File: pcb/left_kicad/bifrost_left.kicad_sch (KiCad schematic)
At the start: 65 parts, among them J1 HRO_TYPE-C-31-M-12, J2 Conn_01x02, J3 Conn_01x06, Q1 AO3401A, Q2 2N7002, Q3 AO3401A, SW1 1.5U, SW10 SW_Push, SW11 SW_Push, SW12 1.25U, SW13 SW_Push, SW14 SW_Push, SW15 SW_Push, SW16 SW_Push, SW17 SW_Push, SW18 SW_Push, SW19 SW_Push, SW2 1.75U, SW20 SW_Push, SW21 SW_Push, SW3 SW_Push, SW4 1.25U, SW5 SW_Push, SW6 SW_Push, SW7 SW_Push, SW8 1.25U, SW9 SW_Push, T1 SW_Push_Shielded, U1 MDBT50Q-1MV2, U2 TP4057, U3 SRV05-4, X1 32.768kHz

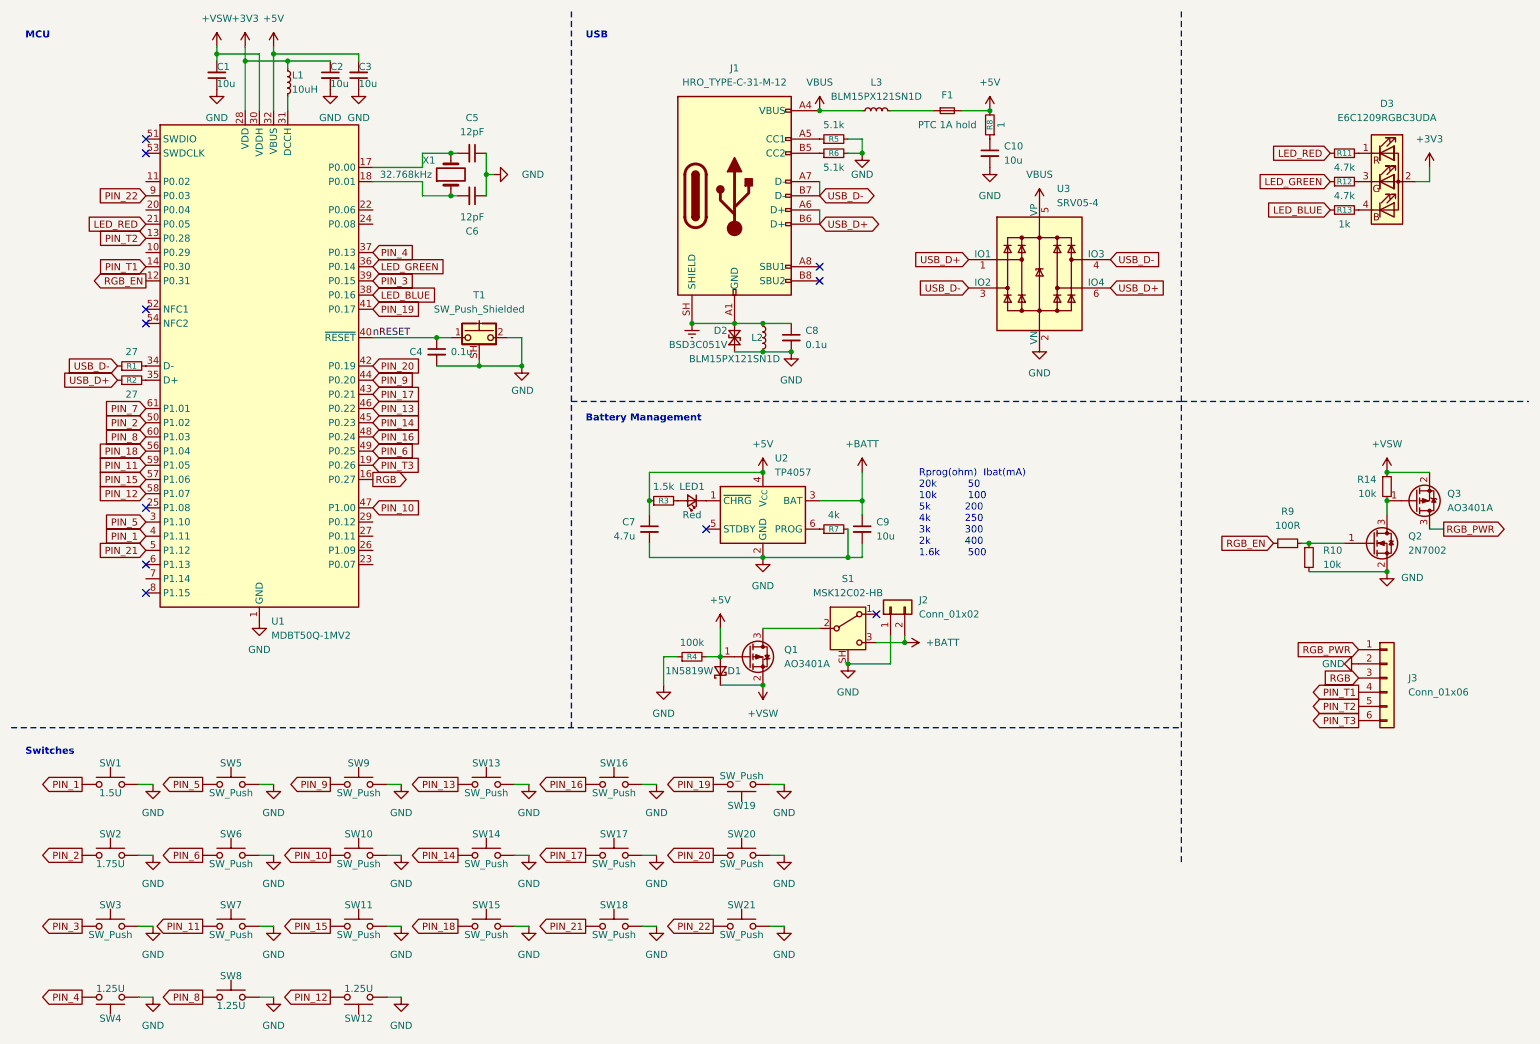
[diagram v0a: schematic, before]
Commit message: Update KiCad keyboard designs
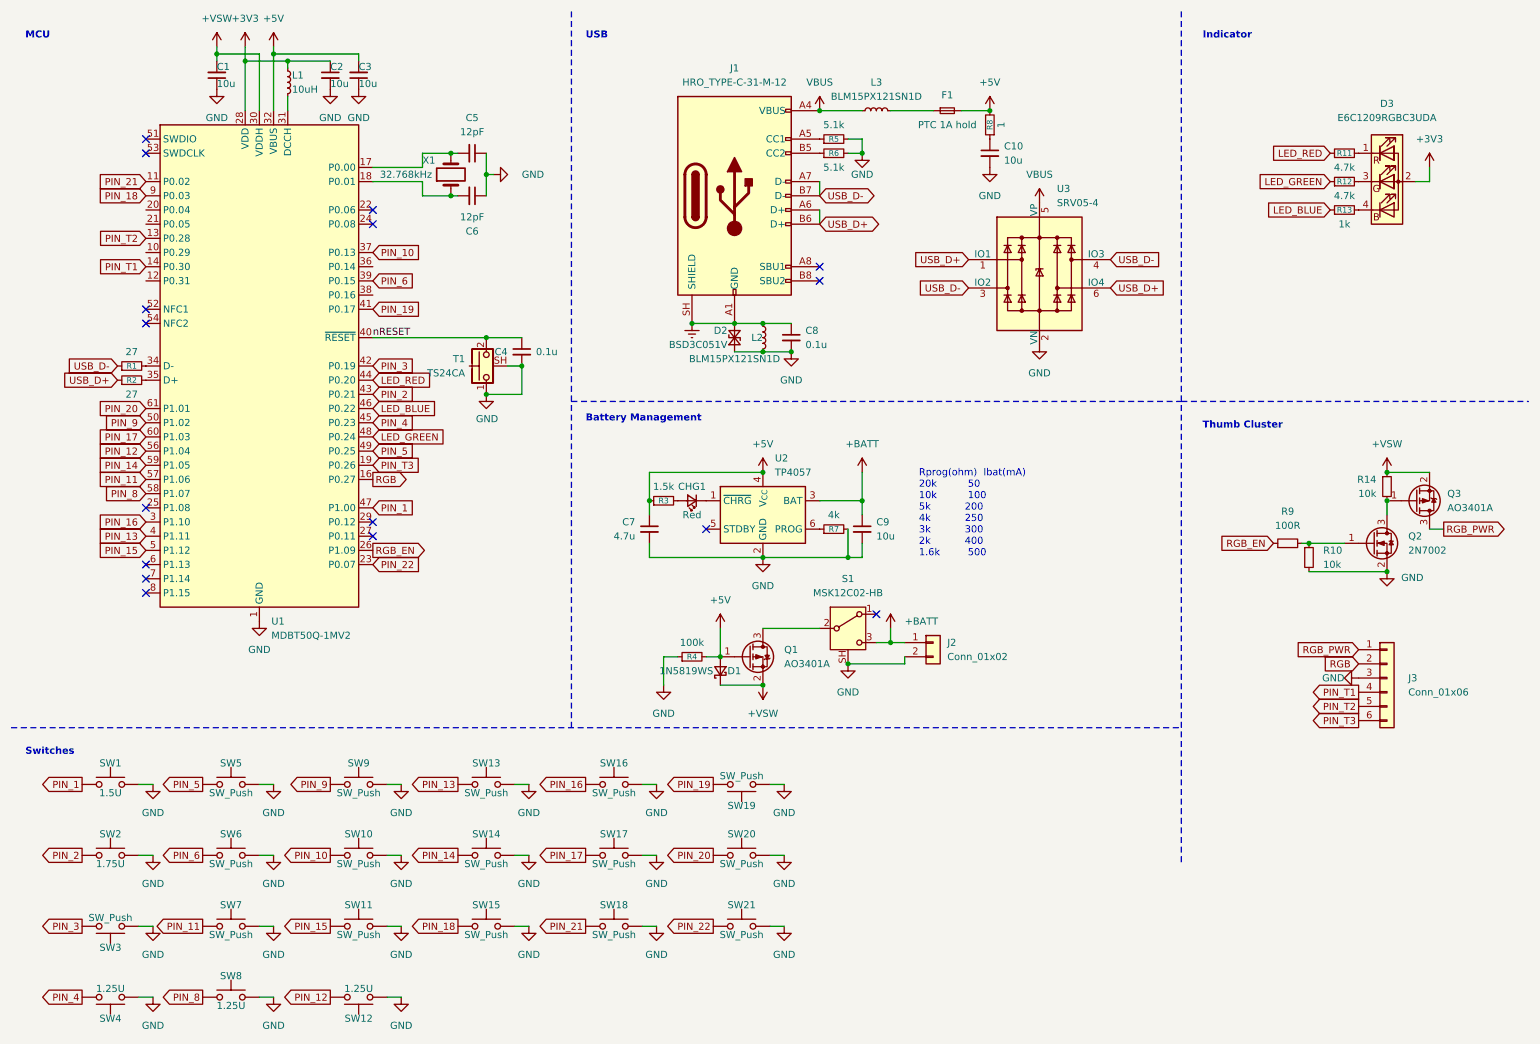
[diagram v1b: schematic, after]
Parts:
- D1: value 1N5819W -> 1N5819WS; footprint Diode_SMD:D_SOD-123 -> Diode_SMD:D_SOD-323
- J2: footprint Connector_Molex:Molex_PicoBlade_53398-0271_1x02-1MP_P1.25mm_Vertical -> Connector_PinHeader_1.27mm:PinHeader_1x02_P1.27mm_Vertical
- J3: footprint Connector_Molex:Molex_PicoBlade_53048-0610_1x06_P1.25mm_Horizontal -> Connector_PinHeader_1.27mm:PinHeader_1x06_P1.27mm_Vertical
- T1: value SW_Push_Shielded -> TS24CA
- renumbered LED1 to CHG1
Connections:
- net PIN_7 is gone; now on net PIN_20: U1.61 (P1.01)
- net +BATT: now also J2.1 (Pin_1); no longer J2.2 (Pin_2)
- net GND: now also J2.2 (Pin_2), J3.3 (Pin_3), SW3.1, T1.1; no longer J2.1 (Pin_1), J3.2 (Pin_2), SW3.2, T1.2
- net LED_BLUE: now also U1.46 (P0.22); no longer U1.38 (P0.16)
- net LED_GREEN: now also U1.48 (P0.24); no longer U1.36 (P0.14)
- net LED_RED: now also U1.44 (P0.20); no longer U1.21 (P0.05)
- net PIN_1: now also U1.47 (P1.00); no longer U1.4 (P1.11)
- net PIN_10: now also U1.37 (P0.13); no longer U1.47 (P1.00)
- net PIN_11: now also U1.57 (P1.06); no longer U1.59 (P1.05)
- net PIN_12: now also U1.56 (P1.04); no longer U1.58 (P1.07)
- net PIN_13: now also U1.4 (P1.11); no longer U1.46 (P0.22)
- net PIN_14: now also U1.59 (P1.05); no longer U1.45 (P0.23)
- net PIN_15: now also U1.5 (P1.12); no longer U1.57 (P1.06)
- net PIN_16: now also U1.3 (P1.10); no longer U1.48 (P0.24)
- net PIN_17: now also U1.60 (P1.03); no longer U1.43 (P0.21)
- net PIN_18: now also U1.9 (P0.03); no longer U1.56 (P1.04)
- net PIN_2: now also U1.43 (P0.21); no longer U1.50 (P1.02)
- net PIN_20: no longer U1.42 (P0.19)
- net PIN_21: now also U1.11 (P0.02); no longer U1.5 (P1.12)
- net PIN_22: now also U1.23 (P0.07); no longer U1.9 (P0.03)
- net PIN_3: now also SW3.2, U1.42 (P0.19); no longer SW3.1, U1.39 (P0.15)
- net PIN_4: now also U1.45 (P0.23); no longer U1.37 (P0.13)
- net PIN_5: now also U1.49 (P0.25); no longer U1.3 (P1.10)
- net PIN_6: now also U1.39 (P0.15); no longer U1.49 (P0.25)
- net PIN_8: now also U1.58 (P1.07); no longer U1.60 (P1.03)
- net PIN_9: now also U1.50 (P1.02); no longer U1.44 (P0.20)
- net RGB: now also J3.2 (Pin_2); no longer J3.3 (Pin_3)
- net RGB_EN: now also U1.26 (P1.09); no longer U1.12 (P0.31)
- net nRESET: now also T1.2; no longer T1.1
- no-connect marks 11 -> 16
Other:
- note added: "Indicator"
- note added: "Thumb Cluster"
- moved on the sheet: C4, J2, SW3, T1

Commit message: Update PCB designs
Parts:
- SW10, SW11, SW13, SW14, SW15, SW16, SW17, SW18, SW19, SW20, SW21, SW5, SW6, SW7, SW9: value SW_Push -> 1U
- SW3: value SW_Push -> 2U
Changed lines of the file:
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@@
 			)
 		)
-		(property "Value" "SW_Push"
+		(property "Value" "2U"
 			(at 30.48 175.006 0)
 			(show_name no)
@@
 			)
 		)
-		(property "Value" "SW_Push"
+		(property "Value" "1U"
 			(at 52.07 152.654 0)
 			(show_name no)
@@
 			)
 		)
-		(property "Value" "SW_Push"
+		(property "Value" "1U"
 			(at 74.93 152.654 0)
 			(show_name no)
@@
 			)
 		)
-		(property "Value" "SW_Push"
+		(property "Value" "1U"
 			(at 97.79 152.654 0)
 			(show_name no)
@@
 			)
 		)
-		(property "Value" "SW_Push"
+		(property "Value" "1U"
 			(at 120.65 152.654 0)
 			(show_name no)
@@
 			)
 		)
-		(property "Value" "SW_Push"
+		(property "Value" "1U"
 			(at 143.51 149.606 0)
 			(show_name no)
@@
 			)
 		)
-		(property "Value" "SW_Push"
+		(property "Value" "1U"
 			(at 143.51 178.054 0)
 			(show_name no)
@@
 			)
 		)
-		(property "Value" "SW_Push"
+		(property "Value" "1U"
 			(at 97.79 178.054 0)
 			(show_name no)
@@
 			)
 		)
-		(property "Value" "SW_Push"
+		(property "Value" "1U"
 			(at 120.65 178.054 0)
 			(show_name no)
@@
 			)
 		)
-		(property "Value" "SW_Push"
+		(property "Value" "1U"
 			(at 52.07 178.054 0)
 			(show_name no)
@@
 			)
 		)
-		(property "Value" "SW_Push"
+		(property "Value" "1U"
 			(at 74.93 178.054 0)
 			(show_name no)
@@
 			)
 		)
-		(property "Value" "SW_Push"
+		(property "Value" "1U"
 			(at 74.93 165.354 0)
 			(show_name no)
@@
 			)
 		)
-		(property "Value" "SW_Push"
+		(property "Value" "1U"
 			(at 52.07 165.354 0)
 			(show_name no)
@@
 			)
 		)
-		(property "Value" "SW_Push"
+		(property "Value" "1U"
 			(at 120.65 165.354 0)
 			(show_name no)
@@
 			)
 		)
-		(property "Value" "SW_Push"
+		(property "Value" "1U"
 			(at 97.79 165.354 0)
 			(show_name no)
@@
 			)
 		)
-		(property "Value" "SW_Push"
+		(property "Value" "1U"
 			(at 143.51 165.354 0)
 			(show_name no)

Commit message: Update PCB BOM and manufacturing outputs
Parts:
- removed C10: 10u, Capacitor_SMD:C_0402_1005Metric, symbol Device:C_Small
- removed R8: 1, Resistor_SMD:R_0402_1005Metric, symbol Device:R_Small
- C1, C2, C3, C9: JLCPCB Part # (none) -> C15525
- C4: renamed from C5; JLCPCB Part # (none) -> C1547
- C5: renamed from C6; JLCPCB Part # (none) -> C1547
- C6: renamed from C4; value 0.1u -> 100n; JLCPCB Part # (none) -> C1525
- C7: JLCPCB Part # (none) -> C23733
- C8: value 0.1u -> 100n; JLCPCB Part # (none) -> C1525
- CHG1: JLCPCB Part # (none) -> C19189741
- D1: renamed from D2; JLCPCB Part # (none) -> C151996
- D2: renamed from D1; JLCPCB Part # (none) -> C191023
- D3: JLCPCB Part # (none) -> C375572
- F1: JLCPCB Part # (none) -> C883131
- J1: JLCPCB Part # (none) -> C51911914
- J2, J3, SW1, SW10, SW11, SW12, SW13, SW14, SW15, SW16, SW17, SW18, SW19, SW2, SW20, SW21, SW3, SW4, SW5, SW6, SW7, SW8, SW9: now left out of the parts list
- L1: footprint Inductor_SMD:L_0402_1005Metric -> Inductor_SMD:L_0603_1608Metric; JLCPCB Part # (none) -> C86083
- L2, L3: JLCPCB Part # (none) -> C88970
- Q1, Q3: JLCPCB Part # (none) -> C15127
- Q2: JLCPCB Part # (none) -> C8545
- R1, R2: JLCPCB Part # (none) -> C25100
- R10: renamed from R11; JLCPCB Part # (none) -> C25900
- R11: renamed from R12; JLCPCB Part # (none) -> C25900
- R12: renamed from R13; JLCPCB Part # (none) -> C11702
- R13: renamed from R14; JLCPCB Part # (none) -> C25744
- R3: JLCPCB Part # (none) -> C25867
- R4: JLCPCB Part # (none) -> C25741
- R5, R6: JLCPCB Part # (none) -> C25905
- R7: value 4k -> 3.3k; JLCPCB Part # (none) -> C25890
- R8: renamed from R9; value 100R -> 100; JLCPCB Part # (none) -> C25076
- R9: renamed from R10; JLCPCB Part # (none) -> C25744
- S1: JLCPCB Part # (none) -> C431541
- T1: JLCPCB Part # (none) -> C393942
- U1: JLCPCB Part # (none) -> C5118826
- U2: JLCPCB Part # (none) -> C12044
- U3: JLCPCB Part # (none) -> C7420376
- X1: JLCPCB Part # (none) -> C32346
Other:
- moved on the sheet: D2, J2, Q1, R4, S1

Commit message: Publish current main PCB manufacturing data
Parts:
- J1: JLCPCB Part # C51911914 -> C165948
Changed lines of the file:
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@@
 			)
 		)
-		(property "JLCPCB Part #" "C51911914"
+		(property "JLCPCB Part #" "C165948"
 			(at 142.24 45.72 0)
 			(hide yes)

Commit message: Refactor application implementation
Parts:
- U2: footprint Package_TO_SOT_SMD:TSOT-23-6 -> Package_TO_SOT_SMD:SOT-23-6
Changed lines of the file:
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@@
 			)
 		)
-		(property "Footprint" "Package_TO_SOT_SMD:TSOT-23-6"
+		(property "Footprint" "Package_TO_SOT_SMD:SOT-23-6"
 			(at 147.32 115.57 0)
 			(hide yes)

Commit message: Update Bifrost case and PCB outputs
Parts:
- added TP1: SWDIO, TestPoint:TestPoint_THTPad_D1.0mm_Drill0.5mm, symbol Connector:TestPoint_Small
- added TP2: SWDCLK, TestPoint:TestPoint_THTPad_D1.0mm_Drill0.5mm, symbol Connector:TestPoint_Small
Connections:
- net GND: now also J3.2 (Pin_2); no longer J3.3 (Pin_3)
- net RGB: now also J3.3 (Pin_3); no longer J3.2 (Pin_2)
- net at U1.51 (SWDIO): now also TP1.1
- net at U1.53 (SWDCLK): now also TP2.1
- no-connect marks 16 -> 14
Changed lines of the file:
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@@
 	)
 	(no_connect
-		(at 36.83 38.1)
-	)
-	(no_connect
 		(at 77.47 50.8)
 	)
@@
 		(at 77.47 106.68)
 	)
-	(no_connect
-		(at 36.83 35.56)
-	)
 	(wire
 		(pts
@@
 	(global_label "RGB"
 		(shape input)
-		(at 254 129.54 180)
+		(at 254 132.08 180)
 		(fields_autoplaced yes)
 		(effects
@@
 		)
 		(property "Intersheetrefs" "${INTERSHEET_REFS}"
-			(at 247.2048 129.54 0)
+			(at 247.2048 132.08 0)
 			(hide yes)
 			(show_name no)
@@
 	)
 	(symbol
+		(lib_id "Connector:TestPoint_Small")
+		(at 36.83 38.1 0)
+		(unit 1)
+		(body_style 1)
+		(exclude_from_sim no)
+		(in_bom yes)
+		(on_board yes)
+		(in_pos_files yes)
+		(dnp no)
+		(property "Reference" "TP2"
+			(at 35.56 38.1 0)
+			(show_name no)
+			(do_not_autoplace no)
+			(effects
+				(font
+					(size 1.27 1.27)
+				)
+				(justify right)
+			)
+		)
+		(property "Value" "SWDCLK"
+			(at 35.56 39.878 0)
+			(show_name no)
+			(do_not_autoplace no)
+			(effects
+				(font
+					(size 1.27 1.27)
+				)
+				(justify right)
+			)
+		)
+		(property "Footprint" "TestPoint:TestPoint_THTPad_D1.0mm_Drill0.5mm"
+			(at 41.91 38.1 0)
+			(hide yes)
+			(show_name no)
+			(do_not_autoplace no)
+			(effects
+				(font
+					(size 1.27 1.27)
+				)
+			)
+		)
+		(property "Datasheet" ""
+			(at 41.91 38.1 0)
+			(hide yes)
+			(show_name no)
+			(do_not_autoplace no)
+			(effects
+				(font
+					(size 1.27 1.27)
+				)
+			)
+		)
+		(property "Description" "test point"
+			(at 36.83 38.1 0)
+			(hide yes)
+			(show_name no)
+			(do_not_autoplace no)
+			(effects
+				(font
+					(size 1.27 1.27)
+				)
+			)
+		)
+		(pin "1"
+		)
+		(instances
+			(project "bifrost_left"
+				(path "/e7e89169-ab7b-68cd-1b0e-3f8776099a22"
+					(reference "TP2")
+					(unit 1)
+				)
+			)
+		)
+	)
+	(symbol
 		(lib_id "Connector_Generic:Conn_01x06")
 		(at 259.08 132.08 0)
@@
 		(lib_name "GND_11")
 		(lib_id "power:GND")
-		(at 254 132.08 270)
+		(at 254 129.54 270)
 		(unit 1)
 		(body_style 1)
@@
 		(fields_autoplaced yes)
 		(property "Reference" "#PWR046"
-			(at 247.65 132.08 0)
+			(at 247.65 129.54 0)
 			(hide yes)
 			(show_name no)
@@
 		)
 		(property "Value" "GND"
-			(at 251.46 132.0799 90)
+			(at 251.46 129.5399 90)
 			(show_name no)
 			(do_not_autoplace no)
@@
 		)
 		(property "Footprint" ""
-			(at 254 132.08 0)
+			(at 254 129.54 0)
 			(hide yes)
 			(show_name no)
@@
 		)
 		(property "Datasheet" ""
-			(at 254 132.08 0)
+			(at 254 129.54 0)
 			(hide yes)
 			(show_name no)
@@
 		)
 		(property "Description" "Power symbol creates a global label with name \"GND\" , ground"
-			(at 254 132.08 0)
+			(at 254 129.54 0)
 			(hide yes)
 			(show_name no)
@@
 					(unit 1)
 				)
+			)
+		)
+	)
+	(symbol
+		(lib_id "Connector:TestPoint_Small")
+		(at 36.83 35.56 180)
+		(unit 1)
+		(body_style 1)
+		(exclude_from_sim no)
+		(in_bom yes)
+		(on_board yes)
+		(in_pos_files yes)
+		(dnp no)
+		(property "Reference" "TP1"
+			(at 35.56 33.782 0)
+			(show_name no)
+			(do_not_autoplace no)
+			(effects
+				(font
+					(size 1.27 1.27)
+				)
+				(justify left)
+			)
+		)
+		(property "Value" "SWDIO"
+			(at 35.56 35.56 0)
+			(show_name no)
+			(do_not_autoplace no)
+			(effects
+				(font
+					(size 1.27 1.27)
+				)
+				(justify left)
+			)
+		)
+		(property "Footprint" "TestPoint:TestPoint_THTPad_D1.0mm_Drill0.5mm"
+			(at 31.75 35.56 0)
+			(hide yes)
+			(show_name no)
+			(do_not_autoplace no)
+			(effects
+				(font
+					(size 1.27 1.27)
+				)
+			)
+		)
+		(property "Datasheet" ""
+			(at 31.75 35.56 0)
+			(hide yes)
+			(show_name no)
+			(do_not_autoplace no)
+			(effects
+				(font
+					(size 1.27 1.27)
+				)
+			)
+		)
+		(property "Description" "test point"
+			(at 36.83 35.56 0)
+			(hide yes)
+			(show_name no)
+			(do_not_autoplace no)
+			(effects
+				(font
+					(size 1.27 1.27)
+				)
+			)
+		)
+		(pin "1"
+		)
+		(instances
+			(project "bifrost_left"
+				(path "/e7e89169-ab7b-68cd-1b0e-3f8776099a22"
+					(reference "TP1")
+					(unit 1)
+				)

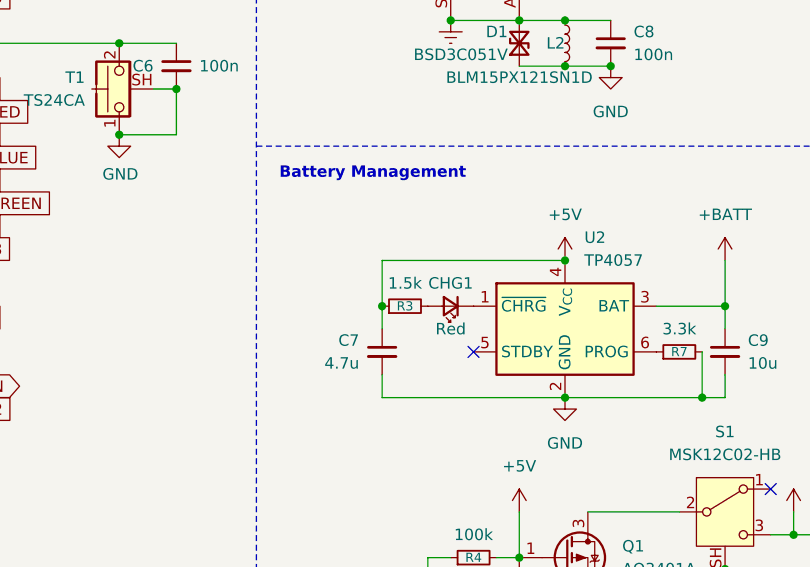
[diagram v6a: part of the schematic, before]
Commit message: Update PCB designs and production files
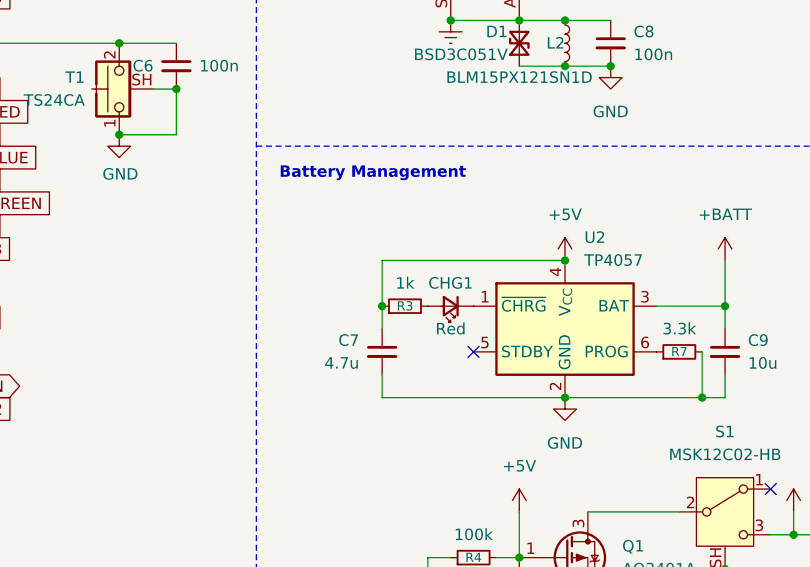
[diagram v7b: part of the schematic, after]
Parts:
- R3: value 1.5k -> 1k; JLCPCB Part # C25867 -> C11702
- X1: JLCPCB Part # C32346 -> C479190
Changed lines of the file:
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@@
 			)
 		)
-		(property "Value" "1.5k"
+		(property "Value" "1k"
 			(at 129.54 97.79 90)
 			(show_name no)
@@
 			)
 		)
-		(property "JLCPCB Part #" "C25867"
+		(property "JLCPCB Part #" "C11702"
 			(at 129.54 100.33 90)
 			(hide yes)
@@
 			)
 		)
-		(property "JLCPCB Part #" "C32346"
+		(property "JLCPCB Part #" "C479190"
 			(at 91.44 41.91 90)
 			(hide yes)

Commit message: Refactor application structure and update implementation
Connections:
- net PIN_22 is gone; now on net PIN_21: SW21.1, U1.23 (P0.07)
- net PIN_11: now also SW11.1, U1.5 (P1.12); no longer SW7.1, U1.57 (P1.06)
- net PIN_15: now also SW15.1, U1.9 (P0.03); no longer SW11.1, U1.5 (P1.12)
- net PIN_18: now also SW18.1, U1.11 (P0.02); no longer SW15.1, U1.9 (P0.03)
- net PIN_21: no longer SW18.1, U1.11 (P0.02)
- new net PIN_7: SW7.1, U1.57 (P1.06)
